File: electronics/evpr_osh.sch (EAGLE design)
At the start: 140 parts

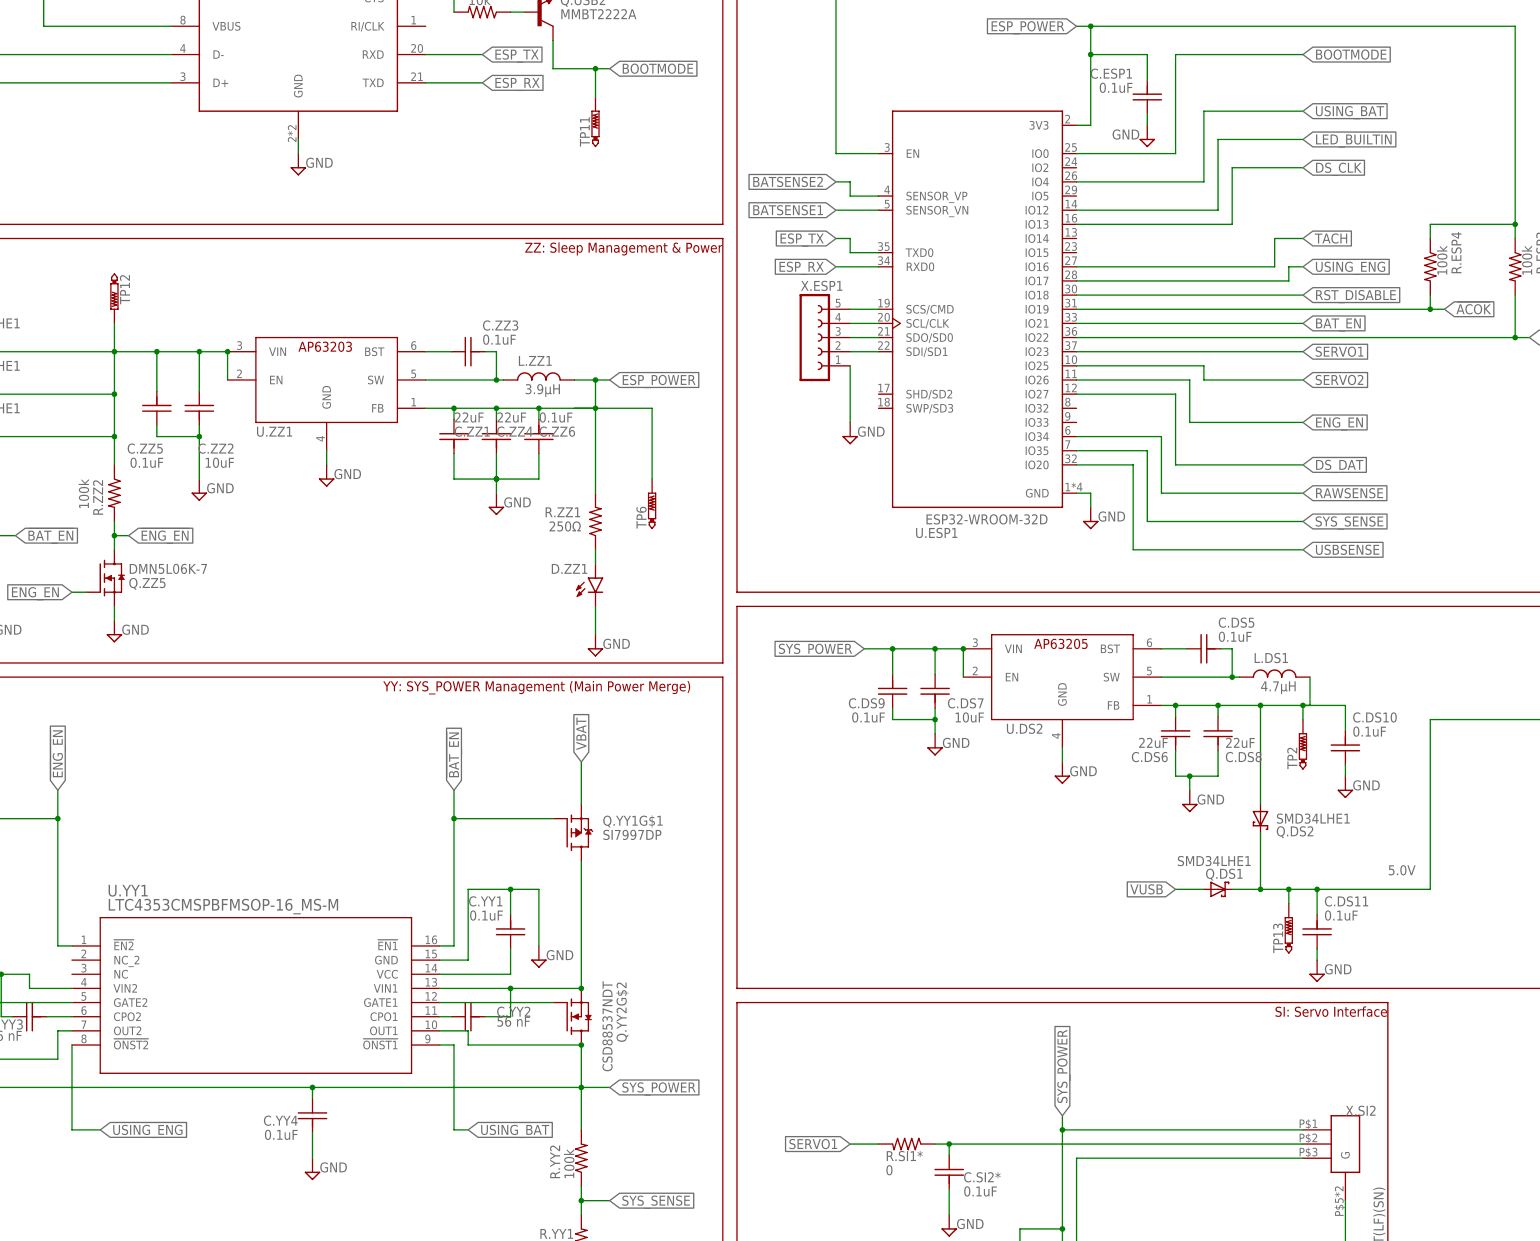
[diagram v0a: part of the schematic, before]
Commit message: Created OSH version with out-of-board holes removed and shims added. Bumped revision to MKII.D
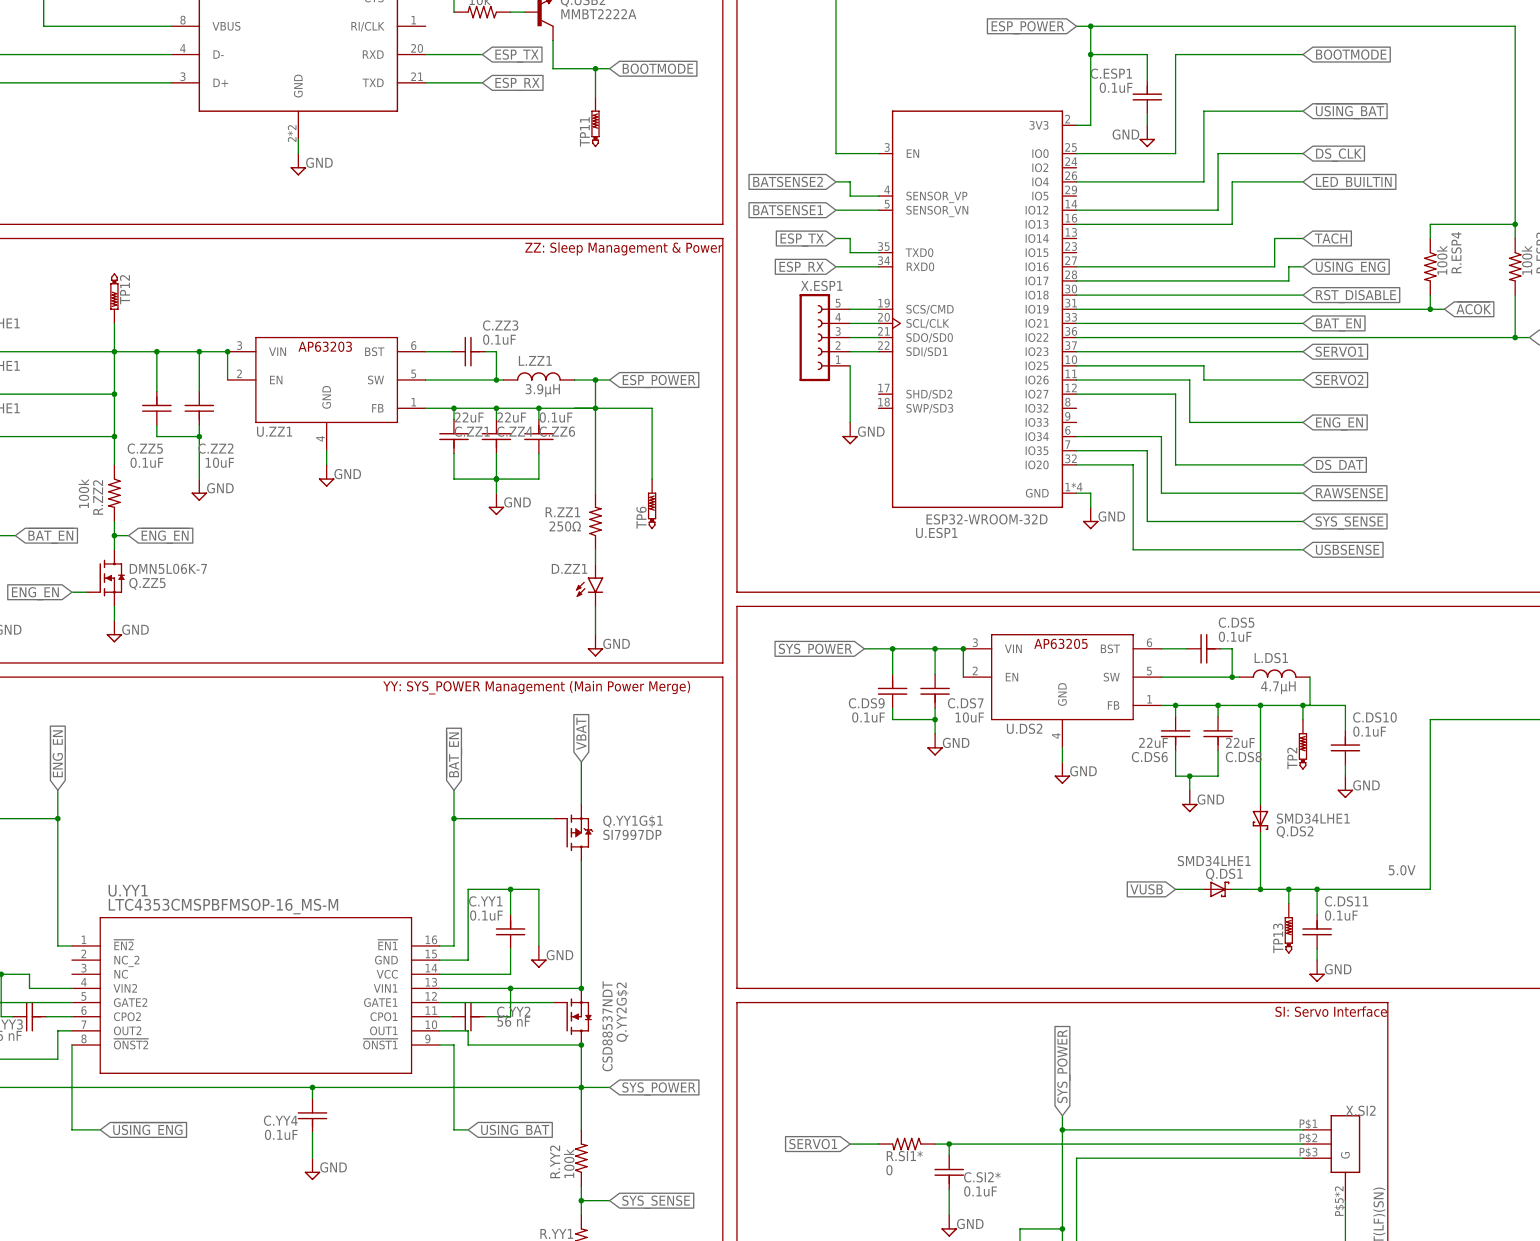
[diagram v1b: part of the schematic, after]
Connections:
- net USING_ENG renamed !USING_ENG
- new net !USING_BAT: U.ESP1.IO4
- net DS_CLK: now also U.ESP1.IO12; no longer U.ESP1.IO13
- net LED_BUILTIN: now also U.ESP1.IO13; no longer U.ESP1.IO12
- net USING_BAT: no longer U.ESP1.IO4
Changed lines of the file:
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@@
 </segment>
 <segment>
-<label x="114.3" y="142.24" size="1.778" layer="95" xref="yes"/>
-<wire x1="101.6" y1="142.24" x2="114.3" y2="142.24" width="0.1524" layer="91"/>
-<pinref part="U.ESP1" gate="G$1" pin="IO13"/>
-<wire x1="73.66" y1="132.08" x2="101.6" y2="132.08" width="0.1524" layer="91"/>
-<wire x1="101.6" y1="132.08" x2="101.6" y2="142.24" width="0.1524" layer="91"/>
+<label x="114.3" y="144.78" size="1.778" layer="95" xref="yes"/>
+<wire x1="99.06" y1="144.78" x2="114.3" y2="144.78" width="0.1524" layer="91"/>
+<pinref part="U.ESP1" gate="G$1" pin="IO12"/>
+<wire x1="99.06" y1="134.62" x2="99.06" y2="144.78" width="0.1524" layer="91"/>
+<wire x1="73.66" y1="134.62" x2="99.06" y2="134.62" width="0.1524" layer="91"/>
 </segment>
 </net>
@@
 </segment>
 </net>
-<net name="USING_ENG" class="0">
+<net name="!USING_ENG" class="0">
 <segment>
 <pinref part="U.YY1" gate="A" pin="!ONST2"/>
@@
 <wire x1="-38.1" y1="-15.24" x2="-38.1" y2="-30.48" width="0.1524" layer="91"/>
 <wire x1="-38.1" y1="-30.48" x2="-35.56" y2="-30.48" width="0.1524" layer="91"/>
-</segment>
-<segment>
-<label x="114.3" y="152.4" size="1.778" layer="95" xref="yes"/>
-<pinref part="U.ESP1" gate="G$1" pin="IO4"/>
-<wire x1="73.66" y1="139.7" x2="96.52" y2="139.7" width="0.1524" layer="91"/>
-<wire x1="96.52" y1="139.7" x2="96.52" y2="152.4" width="0.1524" layer="91"/>
-<wire x1="96.52" y1="152.4" x2="114.3" y2="152.4" width="0.1524" layer="91"/>
 </segment>
 </net>
@@
 <net name="LED_BUILTIN" class="0">
 <segment>
-<pinref part="U.ESP1" gate="G$1" pin="IO12"/>
-<wire x1="73.66" y1="134.62" x2="99.06" y2="134.62" width="0.1524" layer="91"/>
-<wire x1="99.06" y1="134.62" x2="99.06" y2="147.32" width="0.1524" layer="91"/>
-<wire x1="99.06" y1="147.32" x2="114.3" y2="147.32" width="0.1524" layer="91"/>
-<label x="114.3" y="147.32" size="1.778" layer="95" xref="yes"/>
+<wire x1="101.6" y1="132.08" x2="101.6" y2="139.7" width="0.1524" layer="91"/>
+<wire x1="101.6" y1="139.7" x2="114.3" y2="139.7" width="0.1524" layer="91"/>
+<label x="114.3" y="139.7" size="1.778" layer="95" xref="yes"/>
+<pinref part="U.ESP1" gate="G$1" pin="IO13"/>
+<wire x1="73.66" y1="132.08" x2="101.6" y2="132.08" width="0.1524" layer="91"/>
 </segment>
 <segment>
@@
 </segment>
 </net>
+<net name="!USING_BAT" class="0">
+<segment>
+<label x="114.3" y="152.4" size="1.778" layer="95" xref="yes"/>
+<pinref part="U.ESP1" gate="G$1" pin="IO4"/>
+<wire x1="73.66" y1="139.7" x2="96.52" y2="139.7" width="0.1524" layer="91"/>
+<wire x1="96.52" y1="139.7" x2="96.52" y2="152.4" width="0.1524" layer="91"/>
+<wire x1="96.52" y1="152.4" x2="114.3" y2="152.4" width="0.1524" layer="91"/>
+</segment>
+</net>
